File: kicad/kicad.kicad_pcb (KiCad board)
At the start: 2 copper layers, 83.8 x 55.9 mm, 16 parts, among them J1 Conn_01x06_Male, J2 Conn_01x02_Male, J3 Conn_01x02_Male, J4 12V, J5 Relay Switch, U1 4Bit_China_Level_Shifter, U2 WeMos_D1_mini, U3 LTV-817, U4 ULN2803A

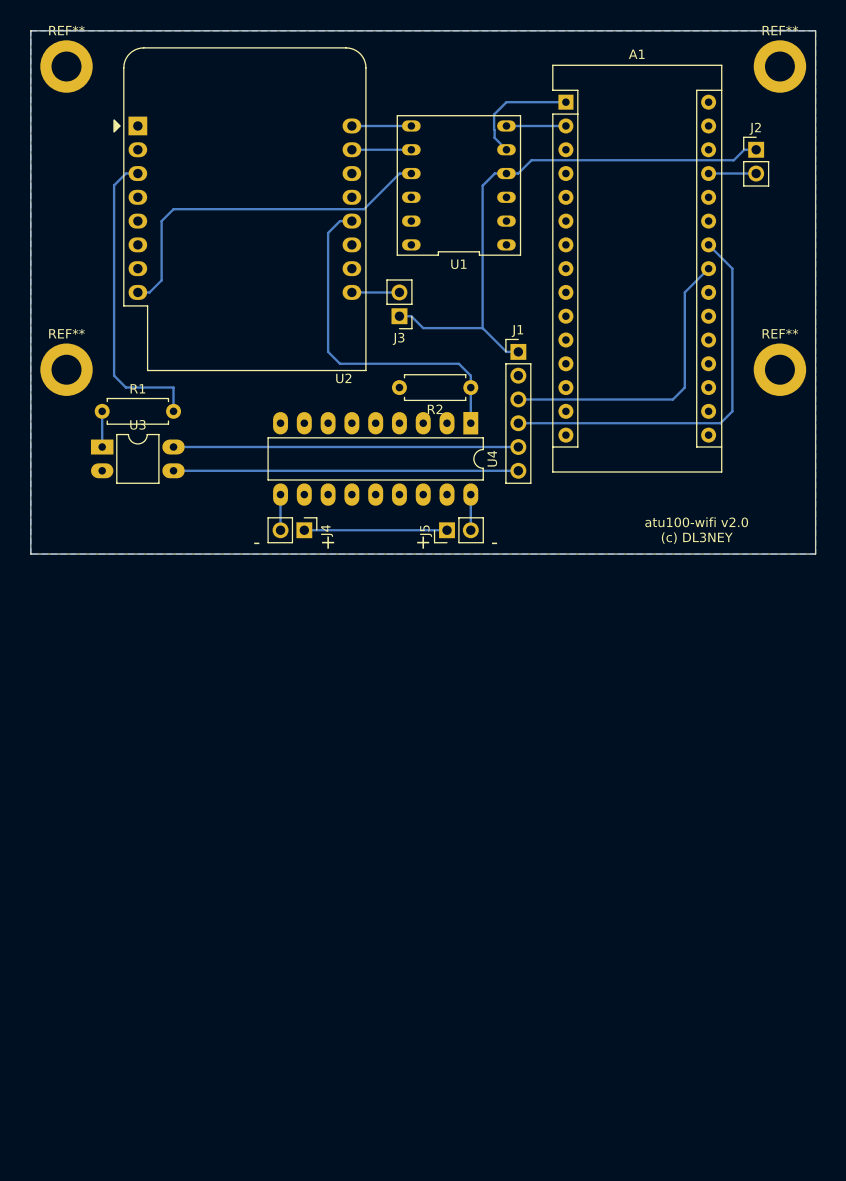
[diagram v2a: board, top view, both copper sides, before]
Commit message: first attempt to leverage all IOs in order to support all three possible buttons and an external antenna switch
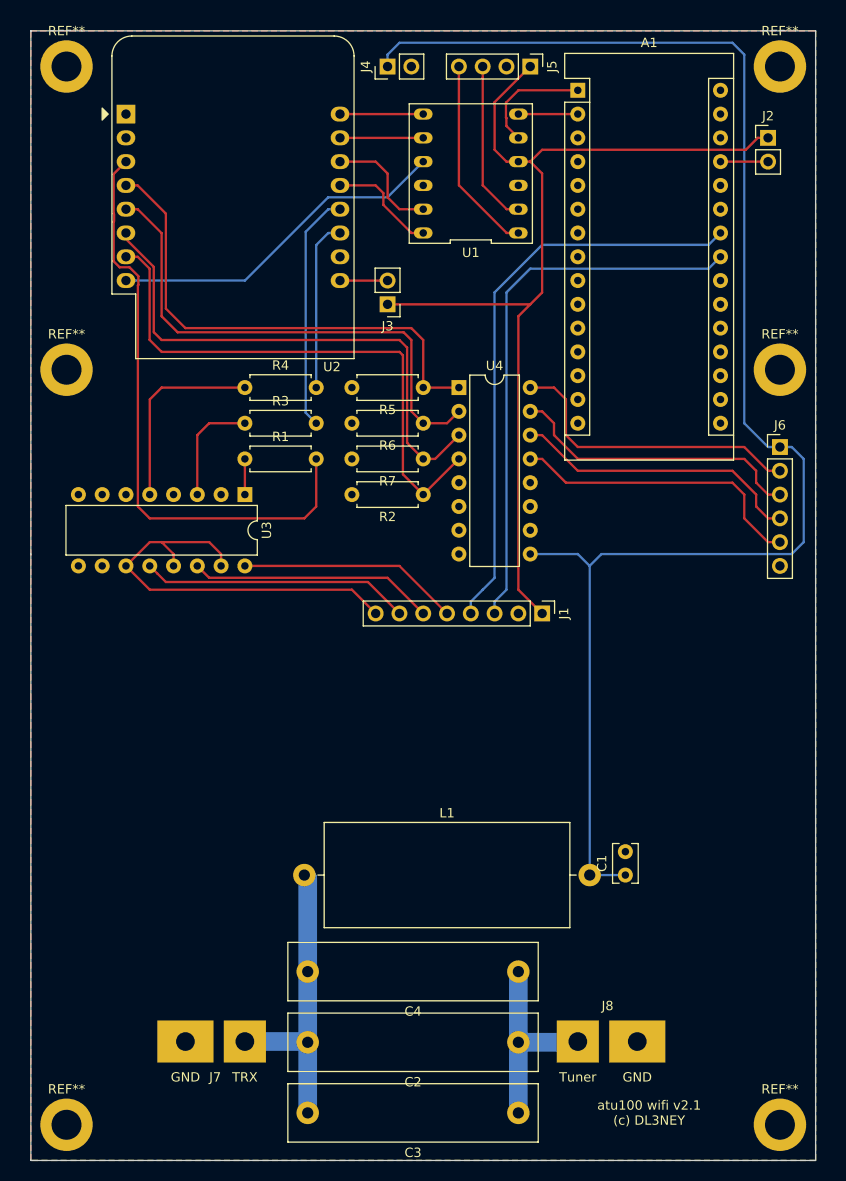
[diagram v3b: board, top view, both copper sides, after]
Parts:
- added C1: 100n, Capacitor_THT:C_Rect_L4.0mm_W2.5mm_P2.50mm, F.Cu at (113.0, 139.7)
- added C2: 10n, Capacitor_THT:C_Rect_L26.5mm_W6.0mm_P22.50mm_MKS4, F.Cu at (101.6, 157.6)
- added C3: 10n, Capacitor_THT:C_Rect_L26.5mm_W6.0mm_P22.50mm_MKS4, F.Cu at (101.6, 165.1)
- added C4: 10n, Capacitor_THT:C_Rect_L26.5mm_W6.0mm_P22.50mm_MKS4, F.Cu at (101.6, 150.0)
- added J6: Ant Switch, Connector_PinHeader_2.54mm:PinHeader_1x06_P2.54mm_Vertical, F.Cu at (129.5, 94.0)
- added J7: TRX, Connector_Wire:SolderWirePad_1x02_P7.62mm_Drill2mm, F.Cu at (72.4, 157.5)
- added J8: Tuner, Connector_Wire:SolderWirePad_1x02_P7.62mm_Drill2mm, F.Cu at (108.0, 157.5)
- added L1: 1m, Inductor_THT:L_Axial_L26.0mm_D11.0mm_P30.48mm_Horizontal_Fastron_77A, F.Cu at (78.7, 139.7)
- added R3: 470, Resistor_THT:R_Axial_DIN0207_L6.3mm_D2.5mm_P7.62mm_Horizontal, F.Cu at (72.4, 91.4)
- added R4: 470, Resistor_THT:R_Axial_DIN0207_L6.3mm_D2.5mm_P7.62mm_Horizontal, F.Cu at (72.4, 87.6)
- added R5: 10k, Resistor_THT:R_Axial_DIN0207_L6.3mm_D2.5mm_P7.62mm_Horizontal, F.Cu at (91.4, 87.6)
- added R6: 10k, Resistor_THT:R_Axial_DIN0207_L6.3mm_D2.5mm_P7.62mm_Horizontal, F.Cu at (91.4, 91.4)
- added R7: 10k, Resistor_THT:R_Axial_DIN0207_L6.3mm_D2.5mm_P7.62mm_Horizontal, F.Cu at (91.4, 95.2)
- added REF**: MountingHole_3.2mm_M3_DIN965_Pad, MountingHole:MountingHole_3.2mm_M3_DIN965_Pad, F.Cu at (129.5, 166.4)
- added REF**: MountingHole_3.2mm_M3_DIN965_Pad, MountingHole:MountingHole_3.2mm_M3_DIN965_Pad, F.Cu at (53.3, 166.4)
- J1: value Conn_01x06_Male -> ATU100; footprint Connector_PinHeader_2.54mm:PinHeader_1x06_P2.54mm_Vertical -> Connector_PinHeader_2.54mm:PinHeader_1x08_P2.54mm_Vertical
- J4: value 12V -> ATU100_12V
- J5: value Relay Switch -> Display/I2C; footprint Connector_PinHeader_2.54mm:PinHeader_1x02_P2.54mm_Vertical -> Connector_PinHeader_2.54mm:PinHeader_1x04_P2.54mm_Vertical
- U3: value LTV-817 -> LTV-847; footprint Package_DIP:DIP-4_W7.62mm_LongPads -> Package_DIP:DIP-16_W7.62mm
- U4: value ULN2803A -> ULN2004A; footprint Package_DIP:DIP-18_W7.62mm_LongPads -> Package_DIP:DIP-16_W7.62mm
- moved J4 50.3 mm to (87.6, 53.3), turned to 90 degrees
- moved J5 50.3 mm to (102.9, 53.3), turned to 270 degrees
- moved J1 28.1 mm to (104.1, 111.8), turned to 270 degrees
- moved R1 16.1 mm to (72.4, 95.2)
- moved U3 16.1 mm to (72.4, 99.1), turned to 270 degrees
- moved R2 12.5 mm to (91.4, 99.1)
- moved U4 4.02 mm to (95.2, 87.6), turned to 0 degrees
- moved J3 1.80 mm to (87.6, 78.7)
- moved J2 1.80 mm to (128.3, 61.0)
- moved U1 1.80 mm to (96.5, 64.8)
- moved U2 1.80 mm to (59.7, 58.4)
- moved A1 1.80 mm to (108.0, 55.9)
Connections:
- net Net-(R1-Pad2) renamed D0
- net Net-(U1-Pad9) renamed +3V3
- J1 pad 5: BTN+ -> BTNTune+
- J1 pad 6: BTN- -> BTNAuto+
- J4 pad 1: Net-(J4-Pad1) -> +12V
- J4 pad 2: Net-(J4-Pad2) -> GND
- J5 pad 1: Net-(J4-Pad1) -> VCC
- J5 pad 2: Net-(J5-Pad2) -> GND
- R2 pad 1: Net-(R2-Pad1) -> D8
- U1 pad 1: Net-(U1-Pad1) -> SCL2
- U1 pad 11: Net-(U1-Pad11) -> D1
- U1 pad 12: Net-(U1-Pad12) -> D2
- U1 pad 2: Net-(U1-Pad2) -> SDA2
- U2 pad 11: Net-(U2-Pad11) -> D4
- U2 pad 12: Net-(R2-Pad1) -> D3
- U2 pad 13: Net-(U2-Pad13) -> D2
- U2 pad 14: Net-(U2-Pad14) -> D1
- U2 pad 4: Net-(U2-Pad4) -> D5
- U2 pad 5: Net-(U2-Pad5) -> D6
- U2 pad 6: Net-(U2-Pad6) -> D7
- U2 pad 7: Net-(U2-Pad7) -> D8
- U3 pad 3: BTN- -> Net-(R3-Pad1)
- U3 pad 4: BTN+ -> GND
- U4 pad 1: Net-(R2-Pad1) -> D5
- U4 pad 10: Net-(J4-Pad2) -> Net-(U4-Pad10)
- U4 pad 13: Net-(U4-Pad13) -> Ant3
- U4 pad 14: Net-(U4-Pad14) -> Ant2
- U4 pad 15: Net-(U4-Pad15) -> Ant1
- U4 pad 16: Net-(U4-Pad16) -> Trafo
- U4 pad 2: Net-(U4-Pad2) -> D6
- U4 pad 3: Net-(U4-Pad3) -> D7
- U4 pad 4: Net-(U4-Pad4) -> D8
- U4 pad 8: Net-(U4-Pad8) -> GND
- U4 pad 9: GND -> +12V
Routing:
- net +12V: track 0.00 -> 164.2 mm
- net D8: track 0.00 -> 59.6 mm
- net D7: track 0.00 -> 57.9 mm
- net D6: track 0.00 -> 55.2 mm
- net D5: track 0.00 -> 53.4 mm
- net VCC: track 60.3 -> 107.4 mm
- net Net-(R2-Pad1): track 37.1 -> 0.00 mm
- net BTN+: track 36.8 -> 0.00 mm
- net Trafo: track 0.00 -> 32.6 mm
- net Net-(C2-Pad2): track 0.00 -> 32.3 mm
- net Ant1: track 0.00 -> 31.8 mm
- net Ant3: track 0.00 -> 31.8 mm
- net D0: track 32.8 -> 64.3 mm
- net Ant2: track 0.00 -> 31.1 mm
- net BTNByp+: track 0.00 -> 28.8 mm
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- added copper zone on F.Cu, net GND
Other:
- board size 83.8 x 55.9 mm -> 83.8 x 120.7 mm
- board text added: "GND"
- board text added: "TRX"
- board text added: "Tuner"
- board text added: "atu100 wifi v2.1 (c) DL3NEY"
- board text removed: "+"
- board text removed: "-"
- board text removed: "atu100-wifi v2.0 (c) DL3NEY"

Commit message: move the 12V connector for the atu100 next to the control signal connector
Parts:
- moved J4 63.7 mm to (113.0, 111.8)
- moved J1 1.27 mm to (105.4, 111.8)
- turned C1 to 270 degrees
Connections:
- REF** pad 1: (no net) -> GND (x6)
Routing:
- net +12V: track 164.2 -> 74.5 mm
- net BTNAuto+: track 26.2 -> 29.0 mm
- net BTNByp+: track 28.8 -> 31.5 mm
- net BTNTune+: track 23.7 -> 26.5 mm
- net +3V3: track 37.0 -> 39.6 mm
- net BTN-: track 44.8 -> 46.9 mm
- net D2: track 11.7 -> 13.7 mm
- net VCC: track 107.4 -> 108.7 mm
- net SCL: track 62.1 -> 61.6 mm
- net SDA: track 59.3 -> 58.7 mm
- net GND: vias 0 -> 38
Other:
- board text added: "12V"
- board text added: "Ant1"
- board text added: "Ant2"
- board text added: "Ant3"
- board text added: "Auto"
- board text added: "BTN-"
- board text added: "Bypass"
- board text added: "SCL"
- board text added: "SDA"
- board text added: "Trafo"
- board text added: "Tune"
- board text added: "VCC"
